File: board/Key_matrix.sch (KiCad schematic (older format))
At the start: 155 parts

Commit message: Fixed the last of the resistors that were using the eagle import schematic symbol
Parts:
- R30, R31, R32, R33, R34, R35: symbol MXKeyboard_RGB-eagle-import:R-EU_R0603 -> Device:R_Small
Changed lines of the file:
@@
 Connection ~ 16500 5650
 Wire Wire Line
-	1100 3500 1000 3500
+	1300 3500 1200 3500
 Wire Wire Line
-	1000 3500 1000 4000
+	1200 3500 1200 4000
 Wire Wire Line
-	1000 4000 1000 4300
+	1200 4000 1200 4300
 Wire Wire Line
-	1000 4300 1000 4600
+	1200 4300 1200 4600
 Wire Wire Line
-	1000 4600 1000 4900
+	1200 4600 1200 4900
 Wire Wire Line
-	1000 4900 1000 5400
+	1200 4900 1200 5400
 Wire Wire Line
-	1000 5400 1000 5500
+	1200 5400 1200 5500
 Wire Wire Line
-	1100 4000 1000 4000
+	1300 4000 1200 4000
 Wire Wire Line
-	1100 4300 1000 4300
+	1300 4300 1200 4300
 Wire Wire Line
-	1100 4600 1000 4600
+	1300 4600 1200 4600
 Wire Wire Line
-	1100 4900 1000 4900
+	1300 4900 1200 4900
 Wire Wire Line
-	1100 5400 1000 5400
-Connection ~ 1000 4000
-Connection ~ 1000 4300
-Connection ~ 1000 4600
-Connection ~ 1000 4900
-Connection ~ 1000 5400
+	1300 5400 1200 5400
+Connection ~ 1200 4000
+Connection ~ 1200 4300
+Connection ~ 1200 4600
+Connection ~ 1200 4900
+Connection ~ 1200 5400
 Wire Wire Line
 	1850 3200 1850 3550
@@
 $EndComp
 $Comp
-L MXKeyboard_RGB-eagle-import:R-EU_R0603 R31
+L Device:R_Small R31
 U 1 1 19BAA81D
-P 1300 4000
+P 1400 4000
 AR Path="/19BAA81D" Ref="R31"  Part="1"
 AR Path="/5F5D4893/19BAA81D" Ref="R31"  Part="1"
-F 0 "R31" H 1250 4059 59  0000 L BNN
-F 1 "20k" H 1400 3930 59  0000 R TNN
-F 2 "rhais_rcl:R0603" H 1300 4000 50  0001 C CNN
-F 3 "" H 1300 4000 50  0001 C CNN
-F 4 "Multicomp" H 1300 4000 59  0001 L BNN "MFR"
-F 5 "MC0063W0603120K5" H 1300 4000 59  0001 L BNN "MPN"
-F 6 "2130963" H 1300 4000 59  0001 L BNN "OC_FARNELL"
-	1    1300 4000
-	1    0    0    -1
+F 0 "R31" V 1350 4000 59  0000 C BNN
+F 1 "20k" V 1450 4000 59  0000 C TNN
+F 2 "rhais_rcl:R0603" H 1400 4000 50  0001 C CNN
+F 3 "" H 1400 4000 50  0001 C CNN
+F 4 "Multicomp" H 1400 4000 59  0001 L BNN "MFR"
+F 5 "MC0063W0603120K5" H 1400 4000 59  0001 L BNN "MPN"
+F 6 "2130963" H 1400 4000 59  0001 L BNN "OC_FARNELL"
+	1    1400 4000
+	0    1    1    0
 $EndComp
 $Comp
-L MXKeyboard_RGB-eagle-import:R-EU_R0603 R32
+L Device:R_Small R32
 U 1 1 A55F53B5
-P 1300 4300
+P 1400 4300
 AR Path="/A55F53B5" Ref="R32"  Part="1"
 AR Path="/5F5D4893/A55F53B5" Ref="R32"  Part="1"
-F 0 "R32" H 1250 4359 59  0000 L BNN
-F 1 "20k" H 1400 4230 59  0000 R TNN
-F 2 "rhais_rcl:R0603" H 1300 4300 50  0001 C CNN
-F 3 "" H 1300 4300 50  0001 C CNN
-F 4 "Multicomp" H 1300 4300 59  0001 L BNN "MFR"
-F 5 "MC0063W0603120K5" H 1300 4300 59  0001 L BNN "MPN"
-F 6 "2130963" H 1300 4300 59  0001 L BNN "OC_FARNELL"
-	1    1300 4300
-	1    0    0    -1
+F 0 "R32" V 1350 4300 59  0000 C BNN
+F 1 "20k" V 1450 4300 59  0000 C TNN
+F 2 "rhais_rcl:R0603" H 1400 4300 50  0001 C CNN
+F 3 "" H 1400 4300 50  0001 C CNN
+F 4 "Multicomp" H 1400 4300 59  0001 L BNN "MFR"
+F 5 "MC0063W0603120K5" H 1400 4300 59  0001 L BNN "MPN"
+F 6 "2130963" H 1400 4300 59  0001 L BNN "OC_FARNELL"
+	1    1400 4300
+	0    1    1    0
 $EndComp
 $Comp
-L MXKeyboard_RGB-eagle-import:R-EU_R0603 R33
+L Device:R_Small R33
 U 1 1 70C53D48
-P 1300 4600
+P 1400 4600
 AR Path="/70C53D48" Ref="R33"  Part="1"
 AR Path="/5F5D4893/70C53D48" Ref="R33"  Part="1"
-F 0 "R33" H 1250 4659 59  0000 L BNN
-F 1 "20k" H 1400 4530 59  0000 R TNN
-F 2 "rhais_rcl:R0603" H 1300 4600 50  0001 C CNN
-F 3 "" H 1300 4600 50  0001 C CNN
-F 4 "Multicomp" H 1300 4600 59  0001 L BNN "MFR"
-F 5 "MC0063W0603120K5" H 1300 4600 59  0001 L BNN "MPN"
-F 6 "2130963" H 1300 4600 59  0001 L BNN "OC_FARNELL"
-	1    1300 4600
-	1    0    0    -1
+F 0 "R33" V 1350 4600 59  0000 C BNN
+F 1 "20k" V 1450 4600 59  0000 C TNN
+F 2 "rhais_rcl:R0603" H 1400 4600 50  0001 C CNN
+F 3 "" H 1400 4600 50  0001 C CNN
+F 4 "Multicomp" H 1400 4600 59  0001 L BNN "MFR"
+F 5 "MC0063W0603120K5" H 1400 4600 59  0001 L BNN "MPN"
+F 6 "2130963" H 1400 4600 59  0001 L BNN "OC_FARNELL"
+	1    1400 4600
+	0    1    1    0
 $EndComp
 $Comp
-L MXKeyboard_RGB-eagle-import:R-EU_R0603 R34
+L Device:R_Small R34
 U 1 1 AD2297CA
-P 1300 4900
+P 1400 4900
 AR Path="/AD2297CA" Ref="R34"  Part="1"
 AR Path="/5F5D4893/AD2297CA" Ref="R34"  Part="1"
-F 0 "R34" H 1250 4959 59  0000 L BNN
-F 1 "20k" H 1400 4830 59  0000 R TNN
-F 2 "rhais_rcl:R0603" H 1300 4900 50  0001 C CNN
-F 3 "" H 1300 4900 50  0001 C CNN
-F 4 "Multicomp" H 1300 4900 59  0001 L BNN "MFR"
-F 5 "MC0063W0603120K5" H 1300 4900 59  0001 L BNN "MPN"
-F 6 "2130963" H 1300 4900 59  0001 L BNN "OC_FARNELL"
-	1    1300 4900
-	1    0    0    -1
+F 0 "R34" V 1350 4959 59  0000 C BNN
+F 1 "20k" V 1450 4900 59  0000 C TNN
+F 2 "rhais_rcl:R0603" H 1400 4900 50  0001 C CNN
+F 3 "" H 1400 4900 50  0001 C CNN
+F 4 "Multicomp" H 1400 4900 59  0001 L BNN "MFR"
+F 5 "MC0063W0603120K5" H 1400 4900 59  0001 L BNN "MPN"
+F 6 "2130963" H 1400 4900 59  0001 L BNN "OC_FARNELL"
+	1    1400 4900
+	0    1    1    0
 $EndComp
 $Comp
-L MXKeyboard_RGB-eagle-import:R-EU_R0603 R35
+L Device:R_Small R35
 U 1 1 357824E1
-P 1300 5400
+P 1400 5400
 AR Path="/357824E1" Ref="R35"  Part="1"
 AR Path="/5F5D4893/357824E1" Ref="R35"  Part="1"
-F 0 "R35" H 1250 5459 59  0000 L BNN
-F 1 "20k" H 1400 5330 59  0000 R TNN
-F 2 "rhais_rcl:R0603" H 1300 5400 50  0001 C CNN
-F 3 "" H 1300 5400 50  0001 C CNN
-F 4 "Multicomp" H 1300 5400 59  0001 L BNN "MFR"
-F 5 "MC0063W0603120K5" H 1300 5400 59  0001 L BNN "MPN"
-F 6 "2130963" H 1300 5400 59  0001 L BNN "OC_FARNELL"
-	1    1300 5400
-	1    0    0    -1
+F 0 "R35" V 1350 5400 59  0000 C BNN
+F 1 "20k" V 1450 5400 59  0000 C TNN
+F 2 "rhais_rcl:R0603" H 1400 5400 50  0001 C CNN
+F 3 "" H 1400 5400 50  0001 C CNN
+F 4 "Multicomp" H 1400 5400 59  0001 L BNN "MFR"
+F 5 "MC0063W0603120K5" H 1400 5400 59  0001 L BNN "MPN"
+F 6 "2130963" H 1400 5400 59  0001 L BNN "OC_FARNELL"
+	1    1400 5400
+	0    1    1    0
 $EndComp
 Text Notes 1600 2400 0    59   ~ 0
@@
 L power:GND #PWR01
 U 1 1 70C1662A
-P 1000 5500
-F 0 "#PWR01" H 1000 5250 50  0001 C CNN
-F 1 "GND" H 1005 5327 50  0000 C CNN
-F 2 "" H 1000 5500 50  0001 C CNN
-F 3 "" H 1000 5500 50  0001 C CNN
-	1    1000 5500
+P 1200 5500
+F 0 "#PWR01" H 1200 5250 50  0001 C CNN
+F 1 "GND" H 1205 5327 50  0000 C CNN
+F 2 "" H 1200 5500 50  0001 C CNN
+F 3 "" H 1200 5500 50  0001 C CNN
+	1    1200 5500
 	1    0    0    -1
 $EndComp
@@
 Connection ~ 1750 5400
 $Comp
-L MXKeyboard_RGB-eagle-import:R-EU_R0603 R30
+L Device:R_Small R30
 U 1 1 B032C944
-P 1300 3500
+P 1400 3500
 AR Path="/B032C944" Ref="R30"  Part="1"
 AR Path="/5F5D4893/B032C944" Ref="R30"  Part="1"
-F 0 "R30" H 1250 3559 59  0000 L BNN
-F 1 "20k" H 1400 3430 59  0000 R TNN
-F 2 "rhais_rcl:R0603" H 1300 3500 50  0001 C CNN
-F 3 "" H 1300 3500 50  0001 C CNN
-F 4 "Multicomp" H 1300 3500 59  0001 L BNN "MFR"
-F 5 "MC0063W0603120K5" H 1300 3500 59  0001 L BNN "MPN"
-F 6 "2130963" H 1300 3500 59  0001 L BNN "OC_FARNELL"
-	1    1300 3500
-	1    0    0    -1
+F 0 "R30" V 1350 3500 59  0000 C BNN
+F 1 "20k" V 1450 3500 59  0000 C TNN
+F 2 "rhais_rcl:R0603" H 1400 3500 50  0001 C CNN
+F 3 "" H 1400 3500 50  0001 C CNN
+F 4 "Multicomp" H 1400 3500 59  0001 L BNN "MFR"
+F 5 "MC0063W0603120K5" H 1400 3500 59  0001 L BNN "MPN"
+F 6 "2130963" H 1400 3500 59  0001 L BNN "OC_FARNELL"
+	1    1400 3500
+	0    1    1    0
 $EndComp
-Wire Wire Line
-	1500 5400 1750 5400
-Wire Wire Line
-	1500 4900 1750 4900
-Wire Wire Line
-	1500 4600 1750 4600
-Wire Wire Line
-	1500 4300 1750 4300
-Wire Wire Line
-	1500 4000 1750 4000
 $Comp
 L power:GND #PWR065
@@
 $EndComp
 Wire Wire Line
+	1500 5400 1750 5400
+Wire Wire Line
+	1500 4900 1750 4900
+Wire Wire Line
+	1500 4600 1750 4600
+Wire Wire Line
+	1500 4300 1750 4300
+Wire Wire Line
+	1500 4000 1750 4000
+Wire Wire Line
 	1500 3500 1750 3500

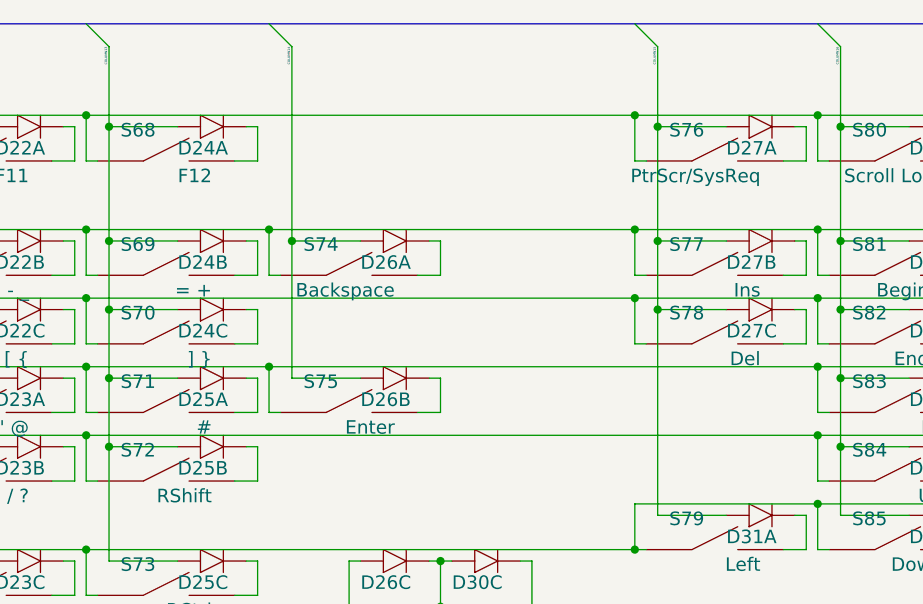
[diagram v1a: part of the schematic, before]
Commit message: Fixed some silkscreen issues and flipped all the LED drivers to use a KiCAD-ified version of the LED driver schematic symbol
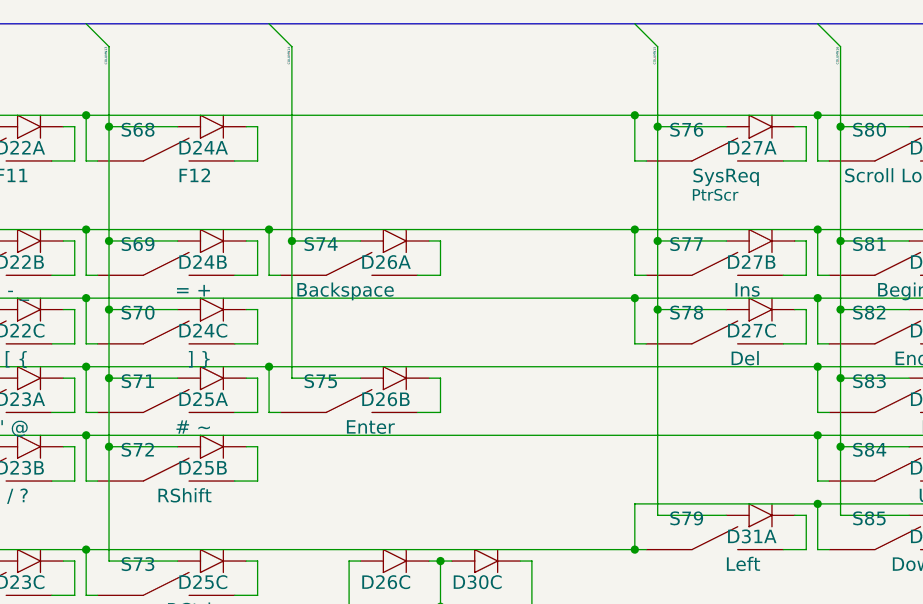
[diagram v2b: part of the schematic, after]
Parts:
- S5: footprint MXKeyboard_RGB:MX_KEY_0.9 -> MXKeyboard_RGB:MX_KEY_1.25u
- S71: value # ~ -> # ~~
- S76: value PtrScr/SysReq -> SysReq; Value2 (none) -> PtrScr
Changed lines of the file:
@@
 F 0 "S5" H 1900 5200 59  0000 L BNN
 F 1 "LShift" H 2300 5000 59  0000 R BNN
-F 2 "MXKeyboard_RGB:MX_KEY_0.9" H 2100 5100 50  0001 C CNN
+F 2 "MXKeyboard_RGB:MX_KEY_1.25u" H 2100 5100 50  0001 C CNN
 F 3 "" H 2100 5100 50  0001 C CNN
 	1    2100 5100
@@
 AR Path="/5F5D4893/5CFD4A7C" Ref="S71"  Part="1"
 F 0 "S71" H 11500 4900 59  0000 L BNN
-F 1 "# ~" H 11900 4700 59  0000 R BNN
+F 1 "# ~~" H 11900 4700 59  0000 R BNN
 F 2 "MXKeyboard_RGB:MX_KEY_NORM" H 11700 4800 50  0001 C CNN
 F 3 "" H 11700 4800 50  0001 C CNN
@@
 AR Path="/5F5D4893/1B7138D8" Ref="S76"  Part="1"
 F 0 "S76" H 13900 3800 59  0000 L BNN
-F 1 "PtrScr/SysReq" H 14300 3600 59  0000 R BNN
+F 1 "SysReq" H 14300 3600 59  0000 R BNN
 F 2 "MXKeyboard_RGB:MX_KEY_NORM" H 14100 3700 50  0001 C CNN
 F 3 "" H 14100 3700 50  0001 C CNN
+F 4 "PtrScr" H 14100 3550 50  0000 C CNN "Value2"
 	1    14100 3700
 	1    0    0    -1

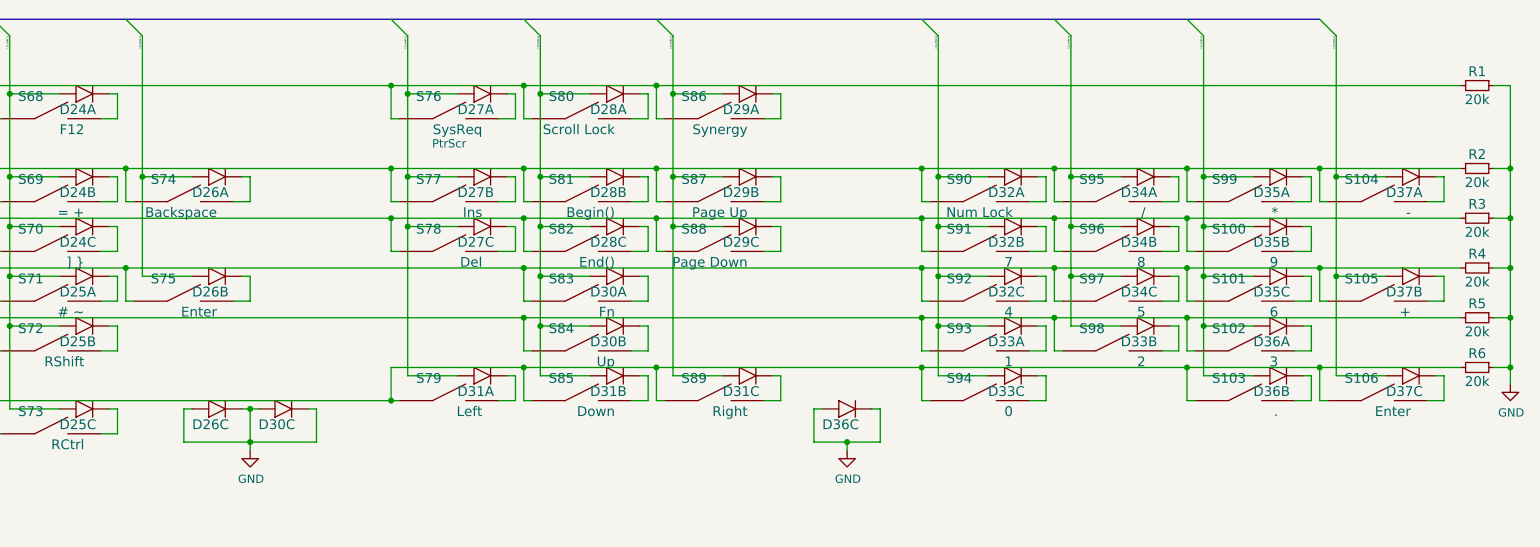
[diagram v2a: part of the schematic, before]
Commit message: Added stabalisers to several of the keys
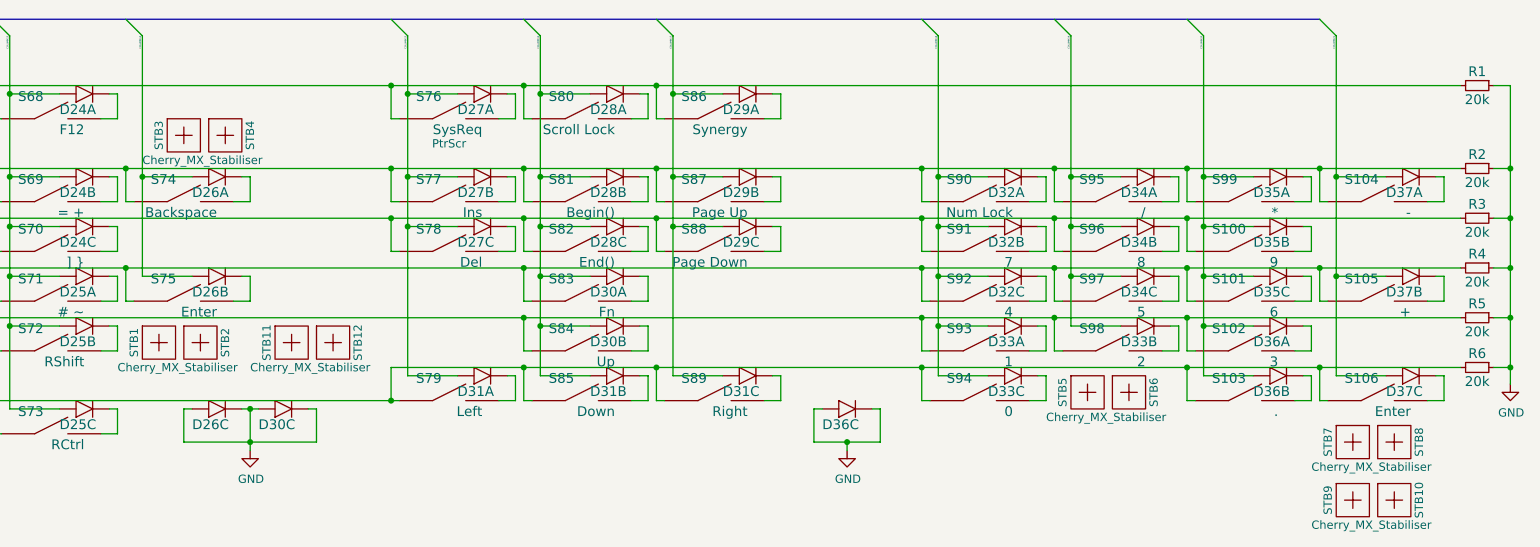
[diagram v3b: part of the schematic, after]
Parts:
- added STB1, STB10, STB11, STB12, STB2, STB3, STB4, STB5, STB6, STB7, STB8, STB9: Cherry_MX_Stabiliser, MXKeyboard_RGB:MX_STABILISER, symbol MXKeyboard_RGB-eagle-import:Cherry_MX_Stabiliser
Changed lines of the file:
@@
 Wire Bus Line
 	1650 3100 19350 3100
+$Comp
+L MXKeyboard_RGB-eagle-import:Cherry_MX_Stabiliser STB1
+U 1 1 9D59DDD9
+P 12350 5050
+F 0 "STB1" V 12200 5050 50  0000 C CNN
+F 1 "Cherry_MX_Stabiliser" H 12100 4900 50  0000 L CNN
+F 2 "MXKeyboard_RGB:MX_STABILISER" H 12350 4800 50  0001 C CNN
+F 3 "" H 12350 5050 50  0001 C CNN
+	1    12350 5050
+	1    0    0    -1
+$EndComp
+$Comp
+L MXKeyboard_RGB-eagle-import:Cherry_MX_Stabiliser STB2
+U 1 1 9D5E9FF4
+P 12600 5050
+F 0 "STB2" V 12750 5050 50  0000 C CNN
+F 1 "Cherry_MX_Stabiliser" H 12728 5005 50  0001 L CNN
+F 2 "MXKeyboard_RGB:MX_STABILISER" H 12600 4800 50  0001 C CNN
+F 3 "" H 12600 5050 50  0001 C CNN
+	1    12600 5050
+	1    0    0    -1
+$EndComp
+$Comp
+L MXKeyboard_RGB-eagle-import:Cherry_MX_Stabiliser STB3
+U 1 1 9D62F4B4
+P 12500 3800
+F 0 "STB3" V 12350 3800 50  0000 C CNN
+F 1 "Cherry_MX_Stabiliser" H 12250 3650 50  0000 L CNN
+F 2 "MXKeyboard_RGB:MX_STABILISER" H 12500 3550 50  0001 C CNN
+F 3 "" H 12500 3800 50  0001 C CNN
+	1    12500 3800
+	1    0    0    -1
+$EndComp
+$Comp
+L MXKeyboard_RGB-eagle-import:Cherry_MX_Stabiliser STB4
+U 1 1 9D6305AF
+P 12750 3800
+F 0 "STB4" V 12900 3800 50  0000 C CNN
+F 1 "Cherry_MX_Stabiliser" H 12878 3755 50  0001 L CNN
+F 2 "MXKeyboard_RGB:MX_STABILISER" H 12750 3550 50  0001 C CNN
+F 3 "" H 12750 3800 50  0001 C CNN
+	1    12750 3800
+	1    0    0    -1
+$EndComp
+$Comp
+L MXKeyboard_RGB-eagle-import:Cherry_MX_Stabiliser STB5
+U 1 1 9D63095A
+P 17950 5350
+F 0 "STB5" V 17800 5350 50  0000 C CNN
+F 1 "Cherry_MX_Stabiliser" H 17700 5200 50  0000 L CNN
+F 2 "MXKeyboard_RGB:MX_STABILISER" H 17950 5100 50  0001 C CNN
+F 3 "" H 17950 5350 50  0001 C CNN
+	1    17950 5350
+	1    0    0    -1
+$EndComp
+$Comp
+L MXKeyboard_RGB-eagle-import:Cherry_MX_Stabiliser STB6
+U 1 1 9D631531
+P 18200 5350
+F 0 "STB6" V 18350 5350 50  0000 C CNN
+F 1 "Cherry_MX_Stabiliser" H 18328 5305 50  0001 L CNN
+F 2 "MXKeyboard_RGB:MX_STABILISER" H 18200 5100 50  0001 C CNN
+F 3 "" H 18200 5350 50  0001 C CNN
+	1    18200 5350
+	1    0    0    -1
+$EndComp
+$Comp
+L MXKeyboard_RGB-eagle-import:Cherry_MX_Stabiliser STB7
+U 1 1 9E908433
+P 19550 5650
+F 0 "STB7" V 19400 5650 50  0000 C CNN
+F 1 "Cherry_MX_Stabiliser" H 19300 5500 50  0000 L CNN
+F 2 "MXKeyboard_RGB:MX_STABILISER" H 19550 5400 50  0001 C CNN
+F 3 "" H 19550 5650 50  0001 C CNN
+	1    19550 5650
+	1    0    0    -1
+$EndComp
+$Comp
+L MXKeyboard_RGB-eagle-import:Cherry_MX_Stabiliser STB8
+U 1 1 9E90908D
+P 19800 5650
+F 0 "STB8" V 19950 5650 50  0000 C CNN
+F 1 "Cherry_MX_Stabiliser" H 19928 5605 50  0001 L CNN
+F 2 "MXKeyboard_RGB:MX_STABILISER" H 19800 5400 50  0001 C CNN
+F 3 "" H 19800 5650 50  0001 C CNN
+	1    19800 5650
+	1    0    0    -1
+$EndComp
+$Comp
+L MXKeyboard_RGB-eagle-import:Cherry_MX_Stabiliser STB9
+U 1 1 9E90DCC1
+P 19550 6000
+F 0 "STB9" V 19400 6000 50  0000 C CNN
+F 1 "Cherry_MX_Stabiliser" H 19300 5850 50  0000 L CNN
+F 2 "MXKeyboard_RGB:MX_STABILISER" H 19550 5750 50  0001 C CNN
+F 3 "" H 19550 6000 50  0001 C CNN
+	1    19550 6000
+	1    0    0    -1
+$EndComp
+$Comp
+L MXKeyboard_RGB-eagle-import:Cherry_MX_Stabiliser STB10
+U 1 1 9E90DEB2
+P 19800 6000
+F 0 "STB10" V 19950 6000 50  0000 C CNN
+F 1 "Cherry_MX_Stabiliser" H 19928 5955 50  0001 L CNN
+F 2 "MXKeyboard_RGB:MX_STABILISER" H 19800 5750 50  0001 C CNN
+F 3 "" H 19800 6000 50  0001 C CNN
+	1    19800 6000
+	1    0    0    -1
+$EndComp
+$Comp
+L MXKeyboard_RGB-eagle-import:Cherry_MX_Stabiliser STB11
+U 1 1 9E9918C2
+P 13150 5050
+F 0 "STB11" V 13000 5050 50  0000 C CNN
+F 1 "Cherry_MX_Stabiliser" H 12900 4900 50  0000 L CNN
+F 2 "MXKeyboard_RGB:MX_STABILISER" H 13150 4800 50  0001 C CNN
+F 3 "" H 13150 5050 50  0001 C CNN
+	1    13150 5050
+	1    0    0    -1
+$EndComp
+$Comp
+L MXKeyboard_RGB-eagle-import:Cherry_MX_Stabiliser STB12
+U 1 1 9E9929B3
+P 13400 5050
+F 0 "STB12" V 13550 5050 50  0000 C CNN
+F 1 "Cherry_MX_Stabiliser" H 13528 5005 50  0001 L CNN
+F 2 "MXKeyboard_RGB:MX_STABILISER" H 13400 4800 50  0001 C CNN
+F 3 "" H 13400 5050 50  0001 C CNN
+	1    13400 5050
+	1    0    0    -1
+$EndComp
 $EndSCHEMATC

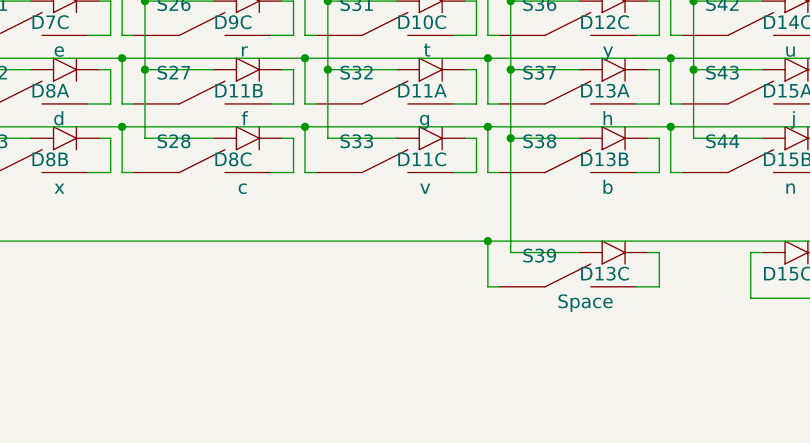
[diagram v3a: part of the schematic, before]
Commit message: Updated all the diodes to use the proper KiCAD package, and added the space bar stabalisers
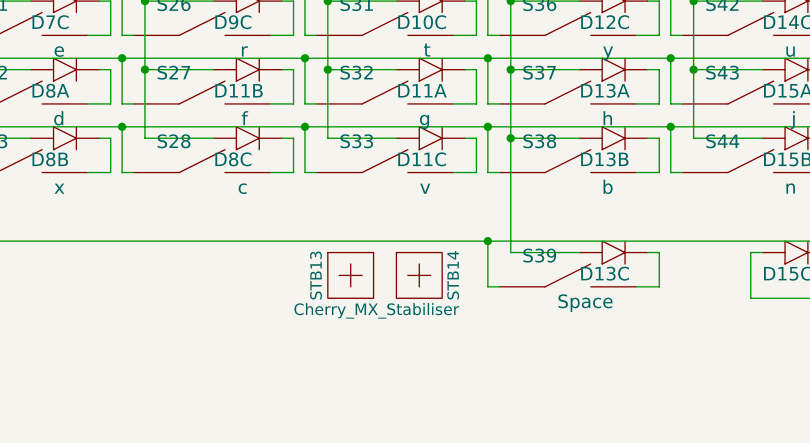
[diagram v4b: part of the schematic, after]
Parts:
- added STB13, STB14: Cherry_MX_Stabiliser, MXKeyboard_RGB:MX_STABILISER, symbol MXKeyboard_RGB-eagle-import:Cherry_MX_Stabiliser
- D1, D10, D11, D12, D13, D14, D15, D16, D17, D18, D19, D2, D20, D21, D22, D23, D24, D25, D26, D27, D28, D29, D3, D30, D31, D32, D33, D34, D35, D36, D37, D4, D5, D6, D7, D8, D9: footprint MXKeyboard_RGB:SOT363_PHILIPS -> rhais_package-smd:SOT-363_SC-70-6
